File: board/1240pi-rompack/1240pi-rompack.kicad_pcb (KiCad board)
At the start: 6 copper layers, 76.2 x 50.8 mm, 23 parts, among them J1 RaspberryPi_CM4_A, J2 RaspberryPi_CM4_B, J3 HDMI_A, J4 HDMI_A, J5 Abracon_ARJM11D7-502-AB-EW2, P1 CardEdge_ROMPACK, U1 74LVC245A, U2 74LVC245A, U3 74LVC245A, U4 74LVC245A

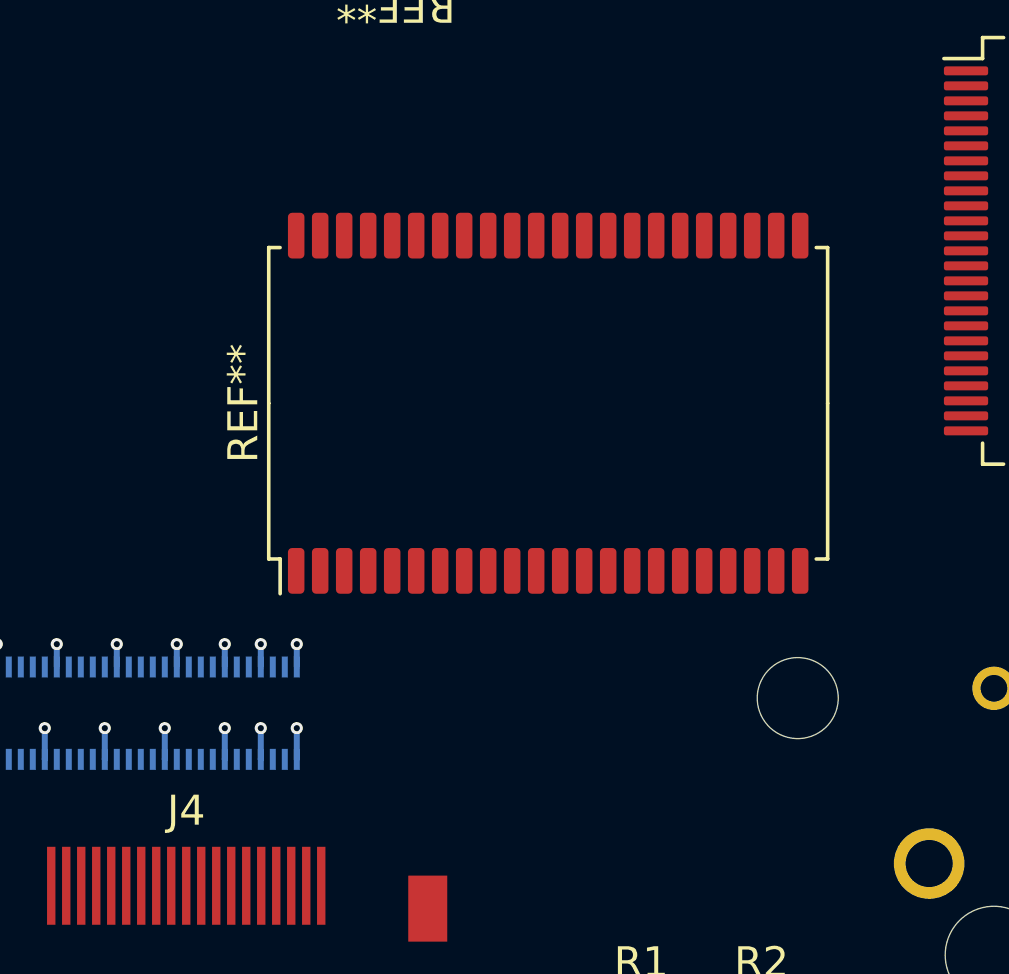
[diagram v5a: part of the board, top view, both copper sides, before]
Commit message: Add footprint for USB daughter board connector.
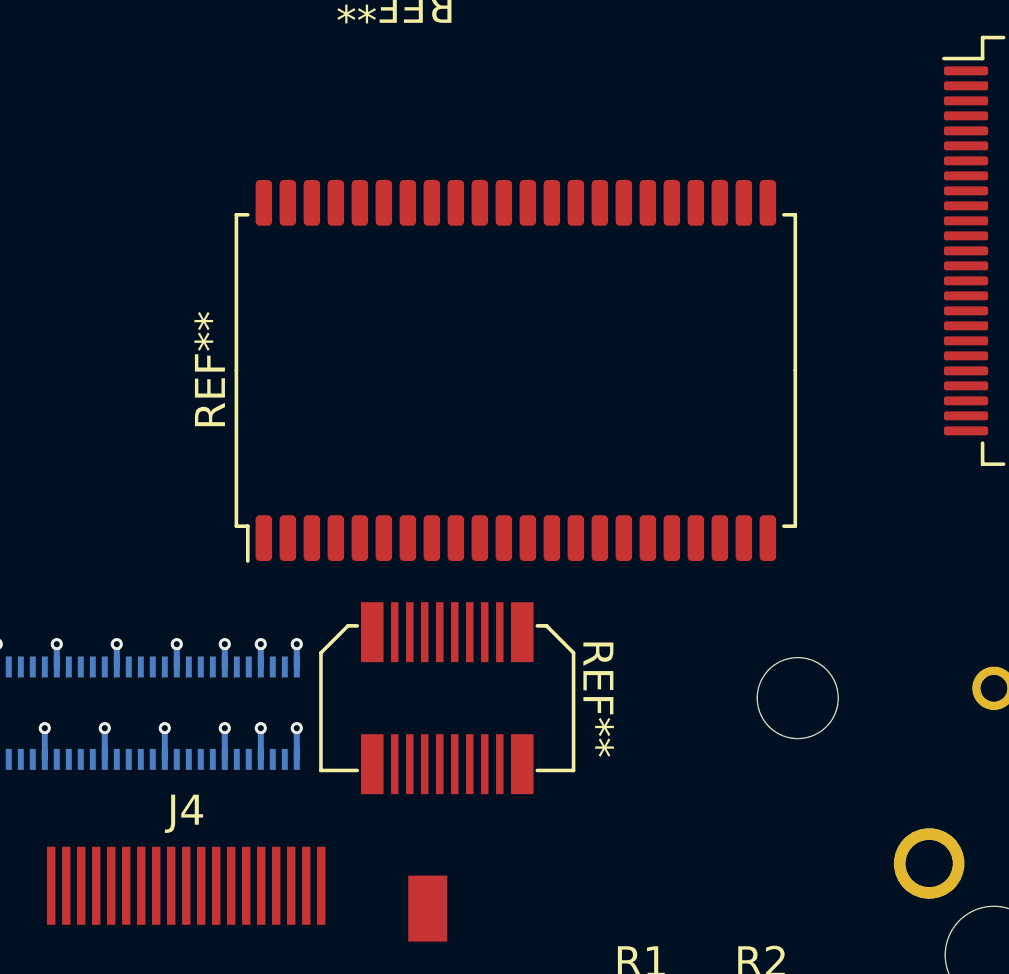
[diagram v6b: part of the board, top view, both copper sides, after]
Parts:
- added REF**: Panasonic_P5KS_Socket, 0Local:Panasonic_AXK5S20247Y, F.Cu at (154.1, 100.0)
- moved REF** 1.53 mm to (156.4, 89.1)
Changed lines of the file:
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@@
     (solder_mask_min_width 0.1016)
     (aux_axis_origin 139.3004 66.5004)
+    (grid_origin 165.800001 100.000001)
     (pcbplotparams
       (layerselection 0x00010fc_ffffffff)
@@
     )
   )
+  (footprint "0Local:Panasonic_AXK5S20247Y" (layer "F.Cu")
+    (at 154.116001 100.000001 -90)
+    (descr "P5KS-series 20-pin mezzanine socket")
+    (attr smd)
+    (fp_text reference "REF**" (at 0 -5 -90 unlocked) (layer "F.SilkS")
+      (effects (font (size 1 1) (thickness 0.15)))
+    )
+    (fp_text value "Panasonic_P5KS_Socket" (at 3 0 unlocked) (layer "F.Fab")
+      (effects (font (size 0.5 0.5) (thickness 0.075)))
+    )
+    (fp_text user "${REFERENCE}" (at 0 0 unlocked) (layer "F.Fab")
+      (effects (font (size 1 1) (thickness 0.15)))
+    )
+    (fp_line (start -1.51 4.21) (end 2.41 4.21) (layer "F.SilkS") (width 0.12))
+    (fp_line (start -2.41 -3.31) (end -1.51 -4.21) (layer "F.SilkS") (width 0.12))
+    (fp_line (start -2.41 3) (end -2.41 3.31) (layer "F.SilkS") (width 0.12))
+    (fp_line (start -2.41 -3) (end -2.41 -3.31) (layer "F.SilkS") (width 0.12))
+    (fp_line (start -2.41 3.31) (end -1.51 4.21) (layer "F.SilkS") (width 0.12))
+    (fp_line (start 2.41 -4.21) (end 2.41 -3) (layer "F.SilkS") (width 0.12))
+    (fp_line (start -1.51 -4.21) (end 2.41 -4.21) (layer "F.SilkS") (width 0.12))
+    (fp_line (start 2.41 4.21) (end 2.41 3) (layer "F.SilkS") (width 0.12))
+    (fp_line (start -2.8 -4.6) (end 2.8 -4.6) (layer "F.CrtYd") (width 0.05))
+    (fp_line (start 2.8 -4.6) (end 2.8 -3.38) (layer "F.CrtYd") (width 0.05))
+    (fp_line (start -2.8 4.6) (end -2.8 3.38) (layer "F.CrtYd") (width 0.05))
+    (fp_line (start 2.8 -3.38) (end 3.7 -3.38) (layer "F.CrtYd") (width 0.05))
+    (fp_line (start 2.8 3.38) (end 2.8 4.6) (layer "F.CrtYd") (width 0.05))
+    (fp_line (start -3.7 -3.38) (end -3.7 3.38) (layer "F.CrtYd") (width 0.05))
+    (fp_line (start -3.7 3.38) (end -2.8 3.38) (layer "F.CrtYd") (width 0.05))
+    (fp_line (start -2.8 -3.38) (end -2.8 -4.6) (layer "F.CrtYd") (width 0.05))
+    (fp_line (start -3.7 -3.38) (end -2.8 -3.38) (layer "F.CrtYd") (width 0.05))
+    (fp_line (start 2.8 4.6) (end -2.8 4.6) (layer "F.CrtYd") (width 0.05))
+    (fp_line (start 2.8 3.38) (end 3.7 3.38) (layer "F.CrtYd") (width 0.05))
+    (fp_line (start 3.7 -3.38) (end 3.7 3.38) (layer "F.CrtYd") (width 0.05))
+    (fp_line (start -2.3 -3.2) (end -1.4 -4.1) (layer "F.Fab") (width 0.1))
+    (fp_line (start 2.3 -4.1) (end 2.3 4.1) (layer "F.Fab") (width 0.1))
+    (fp_line (start 2.3 4.1) (end -1.4 4.1) (layer "F.Fab") (width 0.1))
+    (fp_line (start -2.3 3.2) (end -2.3 -3.2) (layer "F.Fab") (width 0.1))
+    (fp_line (start -1.4 -4.1) (end 2.3 -4.1) (layer "F.Fab") (width 0.1))
+    (fp_line (start -1.4 4.1) (end -2.3 3.2) (layer "F.Fab") (width 0.1))
+    (pad "1" smd rect (at -2.2 -2.5 270) (size 2 0.75) (layers "F.Cu" "F.Paste" "F.Mask"))
+    (pad "2" smd rect (at 2.2 -2.5 270) (size 2 0.75) (layers "F.Cu" "F.Paste" "F.Mask"))
+    (pad "3" smd rect (at -2.2 -1.75 270) (size 2 0.25) (layers "F.Cu" "F.Paste" "F.Mask"))
+    (pad "4" smd rect (at 2.2 -1.75 270) (size 2 0.25) (layers "F.Cu" "F.Paste" "F.Mask"))
+    (pad "5" smd rect (at -2.2 -1.25 270) (size 2 0.25) (layers "F.Cu" "F.Paste" "F.Mask"))
+    (pad "6" smd rect (at 2.2 -1.25 270) (size 2 0.25) (layers "F.Cu" "F.Paste" "F.Mask"))
+    (pad "7" smd rect (at -2.2 -0.75 270) (size 2 0.25) (layers "F.Cu" "F.Paste" "F.Mask"))
+    (pad "8" smd rect (at 2.2 -0.75 270) (size 2 0.25) (layers "F.Cu" "F.Paste" "F.Mask"))
+    (pad "9" smd rect (at -2.2 -0.25 270) (size 2 0.25) (layers "F.Cu" "F.Paste" "F.Mask"))
+    (pad "10" smd rect (at 2.2 -0.25 270) (size 2 0.25) (layers "F.Cu" "F.Paste" "F.Mask"))
+    (pad "11" smd rect (at -2.2 0.25 270) (size 2 0.25) (layers "F.Cu" "F.Paste" "F.Mask"))
+    (pad "12" smd rect (at 2.2 0.25 270) (size 2 0.25) (layers "F.Cu" "F.Paste" "F.Mask"))
+    (pad "13" smd rect (at -2.2 0.75 270) (size 2 0.25) (layers "F.Cu" "F.Paste" "F.Mask"))
+    (pad "14" smd rect (at 2.2 0.75 270) (size 2 0.25) (layers "F.Cu" "F.Paste" "F.Mask"))
+    (pad "15" smd rect (at -2.2 1.25 270) (size 2 0.25) (layers "F.Cu" "F.Paste" "F.Mask"))
+    (pad "16" smd rect (at 2.2 1.25 270) (size 2 0.25) (layers "F.Cu" "F.Paste" "F.Mask"))
+    (pad "17" smd rect (at -2.2 1.75 270) (size 2 0.25) (layers "F.Cu" "F.Paste" "F.Mask"))
+    (pad "18" smd rect (at 2.2 1.75 270) (size 2 0.25) (layers "F.Cu" "F.Paste" "F.Mask"))
+    (pad "19" smd rect (at -2.2 2.5 270) (size 2 0.75) (layers "F.Cu" "F.Paste" "F.Mask"))
+    (pad "20" smd rect (at 2.2 2.5 270) (size 2 0.75) (layers "F.Cu" "F.Paste" "F.Mask"))
+    (model "../local.3dshapes/Panasonic_AXK5S20247Y.stp"
+      (offset (xyz 0 0 0))
+      (scale (xyz 1 1 1))
+      (rotate (xyz 0 0 -90))
+    )
+  )
   (footprint "0Local:Nexperia_SOT764-1" (layer "F.Cu")
     (at 170.942 65.786)
@@
   )
   (footprint "Package_SO:TSOP-II-44_10.16x18.41mm_P0.8mm" (layer "F.Cu")
-    (at 157.48 90.17 90)
+    (at 156.402001 89.078001 90)
     (descr "TSOP-II, 44 Pin (http://www.issi.com/WW/pdf/61-64C5128AL.pdf), generated with kicad-footprint-generator ipc_gullwing_generator.py")
     (tags "TSOP-II SO")

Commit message: Rearrange IO Proc hat, add IO Proc interface.
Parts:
- added C5: 100n, Resistor_SMD:R_0402_1005Metric, F.Cu at (158.9, 79.2)
- added C6: 100n, Resistor_SMD:R_0402_1005Metric, B.Cu at (162.9, 79.2)
- added C7: 100n, Resistor_SMD:R_0402_1005Metric, B.Cu at (154.9, 79.2)
- added C8: 100n, Resistor_SMD:R_0402_1005Metric, B.Cu at (146.9, 78.9)
- added U5: 74LVC245A, 0Local:Nexperia_SOT764-1, B.Cu at (158.9, 78.9)
- added U6: 74LVC245A, 0Local:Nexperia_SOT764-1, F.Cu at (162.9, 78.9)
- added U7: 74LVC245A, 0Local:Nexperia_SOT764-1, F.Cu at (154.9, 78.9)
- added U8: 74LVC245A, 0Local:Nexperia_SOT764-1, F.Cu at (146.9, 78.9)
- J6: renamed from REF**; value Amphenol_62684-50210 -> 62684-50210
- moved REF** 3.25 mm to (159.7, 88.9)
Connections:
- J6 pad 1: (no net) -> /IO Proc Interface/A15
- J6 pad 10: (no net) -> /IO Proc Interface/A6
- J6 pad 11: (no net) -> /IO Proc Interface/A5
- J6 pad 12: (no net) -> /IO Proc Interface/A4
- J6 pad 13: (no net) -> /IO Proc Interface/A3
- J6 pad 14: (no net) -> /IO Proc Interface/A2
- J6 pad 15: (no net) -> /IO Proc Interface/A1
- J6 pad 16: (no net) -> /IO Proc Interface/A0
- J6 pad 17: (no net) -> /IO Proc Interface/D7
- J6 pad 18: (no net) -> /IO Proc Interface/D6
- J6 pad 19: (no net) -> /IO Proc Interface/D5
- J6 pad 2: (no net) -> /IO Proc Interface/A14
- J6 pad 20: (no net) -> /IO Proc Interface/D4
- J6 pad 21: (no net) -> /IO Proc Interface/D3
- J6 pad 22: (no net) -> /IO Proc Interface/D2
- J6 pad 23: (no net) -> /IO Proc Interface/D1
- J6 pad 24: (no net) -> /IO Proc Interface/D0
- J6 pad 25: (no net) -> unconnected-(J6-Pad25)
- J6 pad 26: (no net) -> GND
- J6 pad 27: (no net) -> /IO Proc Interface/~{WR}
- J6 pad 28: (no net) -> /IO Proc Interface/~{MREQ}
- J6 pad 29: (no net) -> /IO Proc Interface/~{RD}
- J6 pad 3: (no net) -> /IO Proc Interface/A13
- J6 pad 30: (no net) -> /IO Proc Interface/~{BUSREQ}
- J6 pad 31: (no net) -> /IO Proc Interface/~{RESET}
- J6 pad 32: (no net) -> /IO Proc Interface/~{NMI}
- J6 pad 33: (no net) -> /IO Proc Interface/~{INT}
- J6 pad 34: (no net) -> /IO Proc Interface/~{WAIT}
- J6 pad 35: (no net) -> /IO Proc Interface/~{BUSACK}
- J6 pad 36: (no net) -> /IO Proc Interface/~{CLK}
- J6 pad 37: (no net) -> /IO Proc Interface/~{RFSH}
- J6 pad 38: (no net) -> /IO Proc Interface/~{M1}
- J6 pad 39: (no net) -> /IO Proc Interface/~{IORQ}
- J6 pad 4: (no net) -> /IO Proc Interface/A12
- J6 pad 40: (no net) -> /IO Proc Interface/~{HALT}
- J6 pad 5: (no net) -> /IO Proc Interface/A11
- J6 pad 6: (no net) -> /IO Proc Interface/A10
- J6 pad 7: (no net) -> /IO Proc Interface/A9
- J6 pad 8: (no net) -> /IO Proc Interface/A8
- J6 pad 9: (no net) -> /IO Proc Interface/A7
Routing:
- net GND: track 80.8 -> 106.9 mm, vias 95 -> 100
- net +3V3: track 8.89 -> 20.2 mm, vias 4 -> 8
- net /IO Proc Interface/~{WAIT}: track 0.00 -> 2.10 mm
- net /IO Proc Interface/~{RFSH}: track 0.00 -> 2.10 mm
- net /IO Proc Interface/~{M1}: track 0.00 -> 2.10 mm
- net /IO Proc Interface/~{IORQ}: track 0.00 -> 2.10 mm
- net /IO Proc Interface/~{INT}: track 0.00 -> 2.10 mm
- net /IO Proc Interface/~{HALT}: track 0.00 -> 2.10 mm
- net /IO Proc Interface/~{CLK}: track 0.00 -> 2.10 mm
- net /IO Proc Interface/~{BUSACK}: track 0.00 -> 2.10 mm
- net /IO Proc Interface/D7: track 0.00 -> 2.10 mm
- net /IO Proc Interface/D6: track 0.00 -> 2.10 mm
- net /IO Proc Interface/D5: track 0.00 -> 2.10 mm
- net /IO Proc Interface/D4: track 0.00 -> 2.10 mm
- net /IO Proc Interface/D3: track 0.00 -> 2.10 mm
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
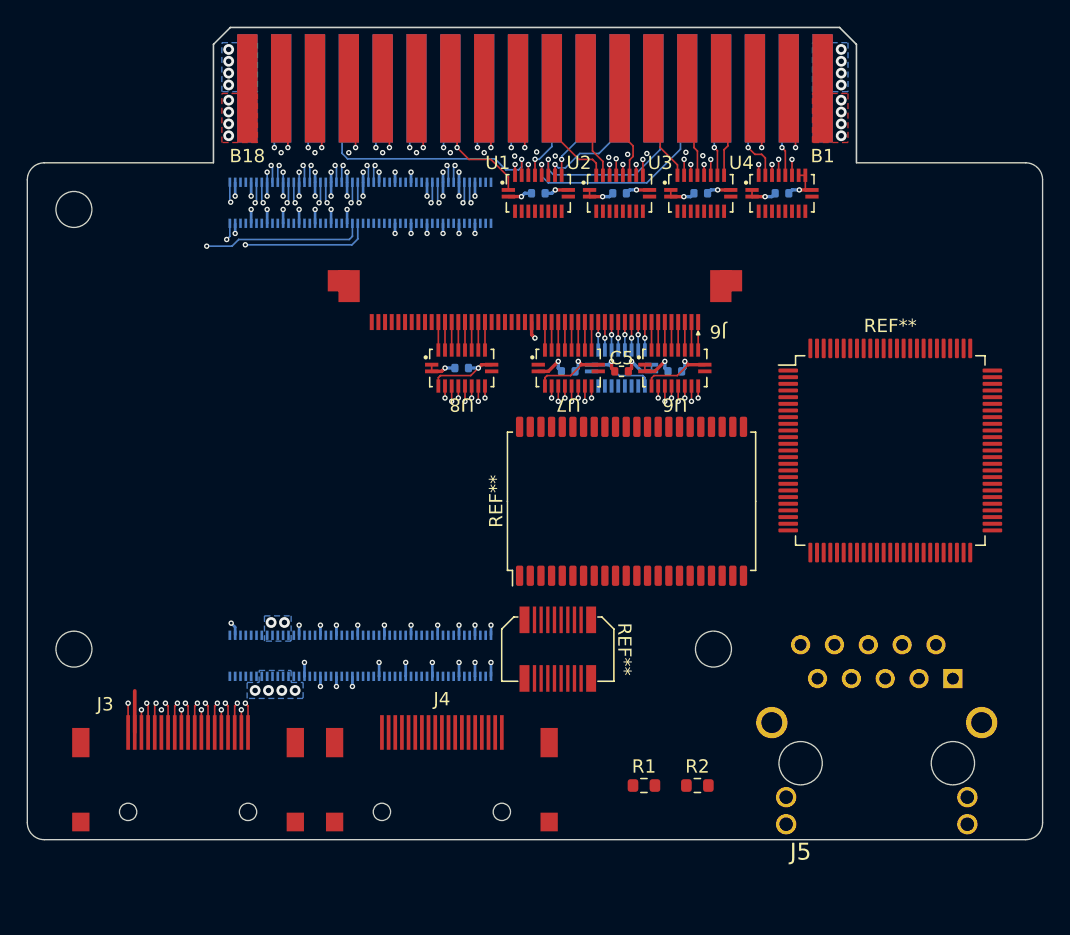
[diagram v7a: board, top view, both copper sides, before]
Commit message: Reroute IO Proc hat again and add buffers on rompack board.
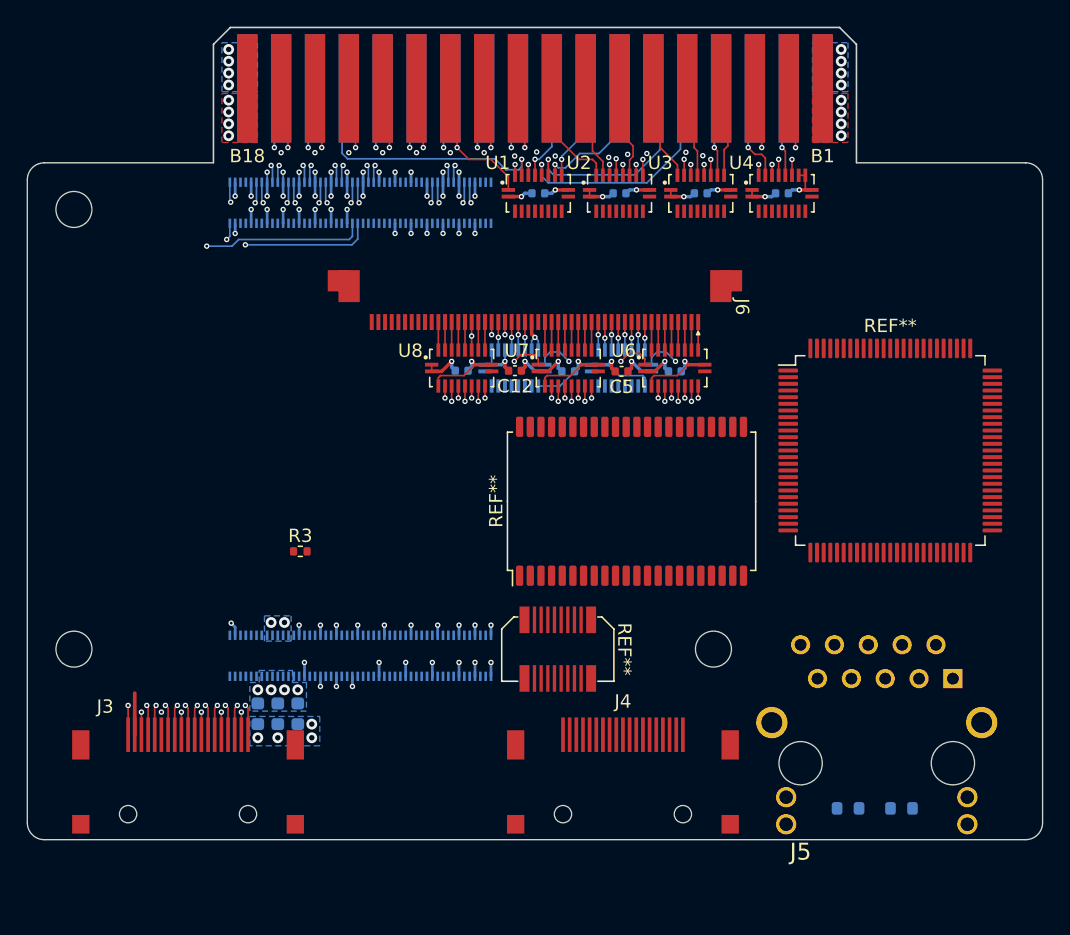
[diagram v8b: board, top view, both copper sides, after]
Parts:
- added C10: 100n, Capacitor_SMD:C_0603_1608Metric, B.Cu at (133.1, 104.9)
- added C11: 100n, Capacitor_SMD:C_0603_1608Metric, B.Cu at (134.6, 104.9)
- added C12: 100n, Capacitor_SMD:C_0402_1005Metric, F.Cu at (150.9, 79.1)
- added C9: 100n, Capacitor_SMD:C_0603_1608Metric, B.Cu at (131.6, 104.9)
- added R3: 10k, Resistor_SMD:R_0402_1005Metric, F.Cu at (134.8, 92.7)
- added U9: 74LVC245A, 0Local:Nexperia_SOT764-1, B.Cu at (150.9, 78.9)
- C1, C2, C3, C4, C5, C6, C7, C8: footprint Resistor_SMD:R_0402_1005Metric -> Capacitor_SMD:C_0402_1005Metric
- R1, R2: moved to B.Cu
- moved R1 19.4 mm to (179.9, 112.0), turned to 180 degrees
- moved J4 13.6 mm to (159.0, 106.4)
- moved R2 11.4 mm to (175.9, 112.0), turned to 180 degrees
- moved C8 0.20 mm to (146.9, 79.1)
- moved J3 0.17 mm to (126.4, 106.4)
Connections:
- net /IO Proc Interface/~{IIORQ} renamed /IO Proc Interface/~{IRESET}
- J6 pad 31: /IO Proc Interface/~{RESET} -> /IO Proc Interface/~{IORQ}
- J6 pad 39: /IO Proc Interface/~{IORQ} -> /IO Proc Interface/~{RESET}
- U5 pad 1: +3V3 -> /IO Proc Interface/~{BUSACK}
- U6 pad 1: +3V3 -> /IO Proc Interface/~{BUSACK}
- U7 pad 1: unconnected-(U7-Pad1) -> /IO Proc Interface/~{IDOUT}
- U8 pad 3: /IO Proc Interface/~{IORQ} -> /IO Proc Interface/~{RESET}
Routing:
- net /IO Proc Interface/~{BUSACK}: track 2.10 -> 28.1 mm, vias 0 -> 4
- net GND: track 106.9 -> 117.0 mm, vias 100 -> 105
- net /IO Proc Interface/~{IDOUT}: track 0.00 -> 2.58 mm, vias 0 -> 1
- net +3V3: track 20.2 -> 22.6 mm, vias 8 -> 9
- net /IO Proc Interface/~{WR}: track 0.00 -> 2.10 mm, vias 0 -> 1
- net /IO Proc Interface/~{RESET}: track 0.00 -> 2.10 mm
- net /IO Proc Interface/~{RD}: track 0.00 -> 2.10 mm, vias 0 -> 1
- net /IO Proc Interface/~{MREQ}: track 0.00 -> 2.10 mm, vias 0 -> 1
- net /IO Proc Interface/~{NMI}: track 0.00 -> 0.95 mm, vias 0 -> 1
- net /IO Proc Interface/~{BUSREQ}: track 0.00 -> 0.95 mm, vias 0 -> 1
- net /IO Proc Interface/~{IORQ}: vias 0 -> 1
